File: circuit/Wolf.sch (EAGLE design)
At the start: 25 parts, among them IC1 74LS595N, IC2 24LC256P, K1 SNES, M1 ARDUINO-NANO-3.0

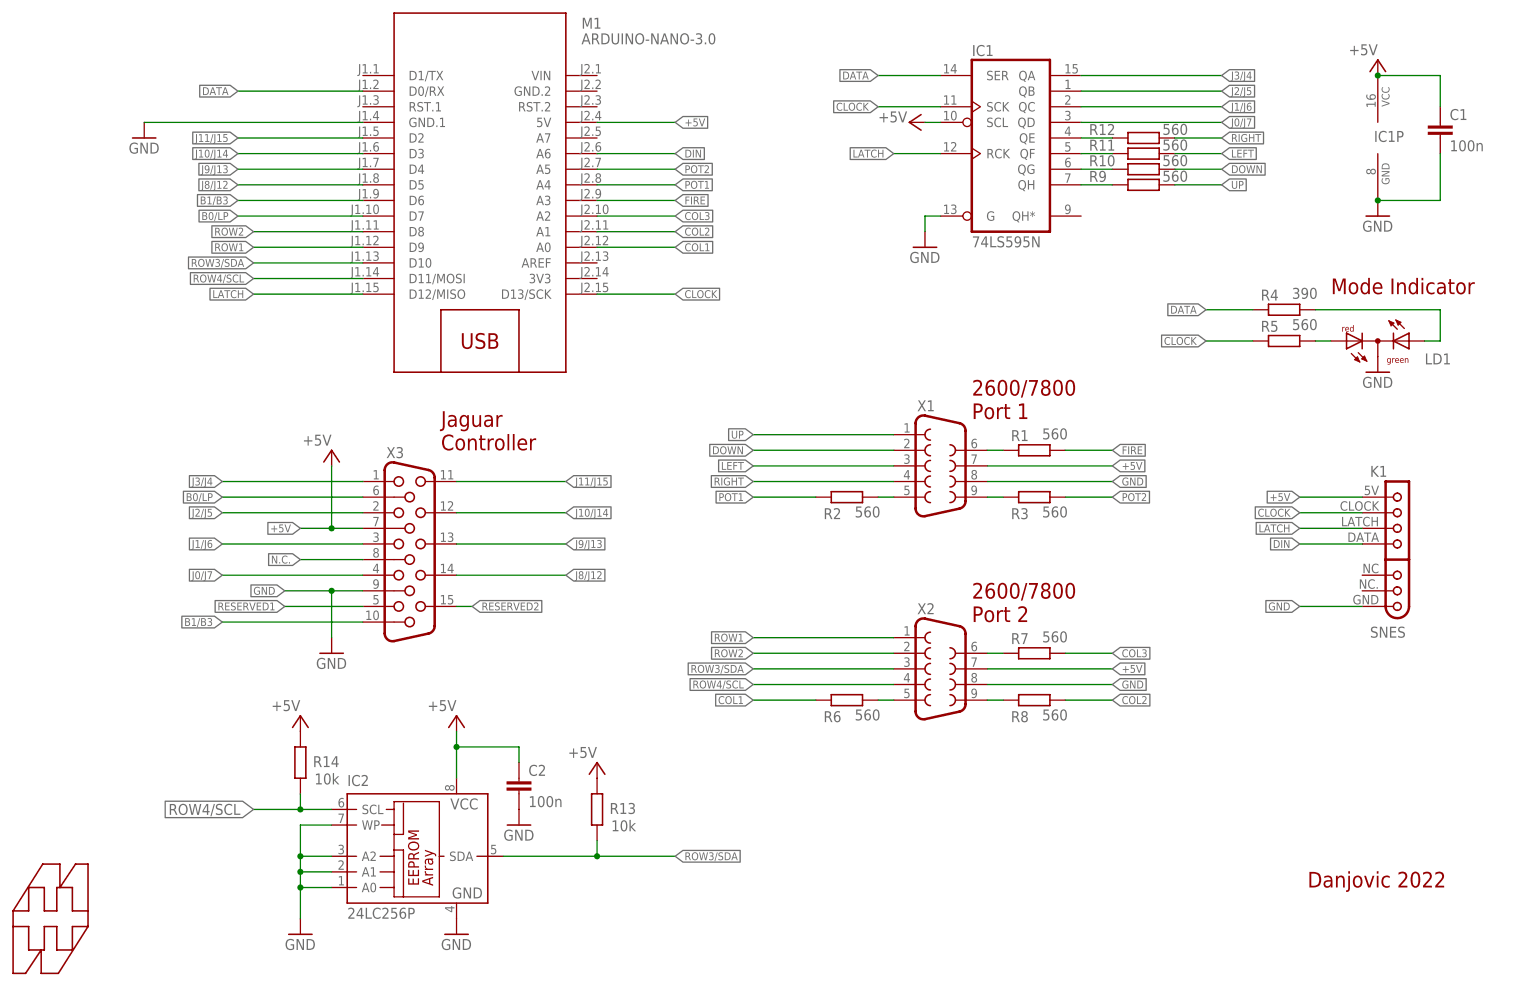
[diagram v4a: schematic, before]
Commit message: Added neopixel to indicate operating mode
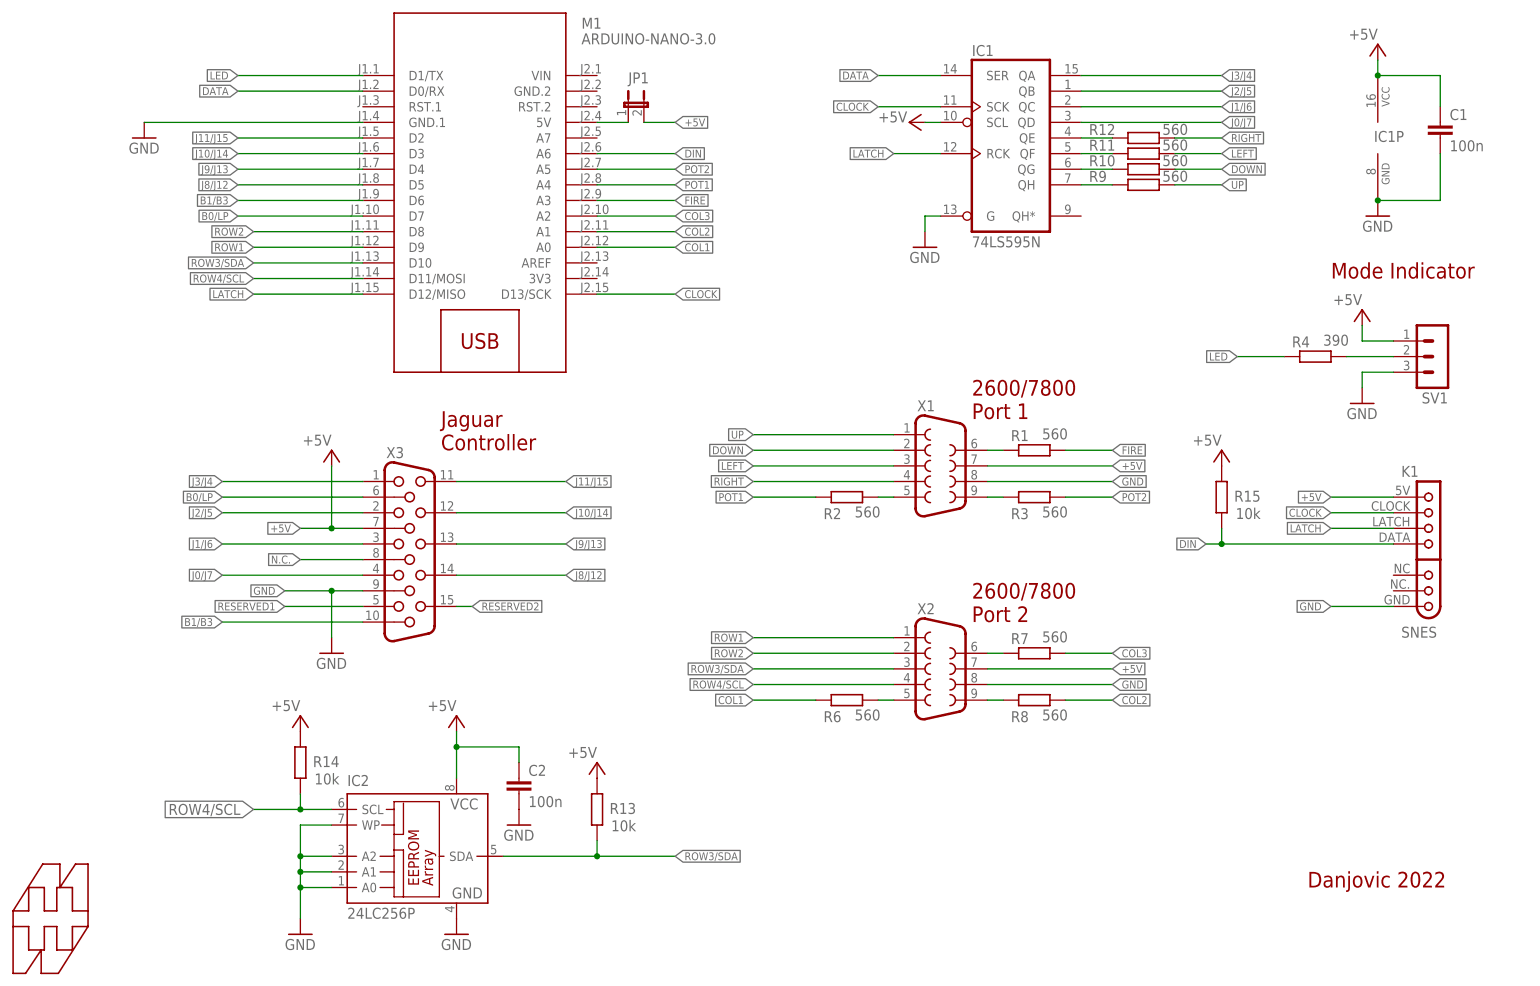
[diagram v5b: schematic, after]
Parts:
- removed LD1: (no value), led:DUOLED-RG-C
- removed R5: 560, rcl:R-EU_0204/7
- added JP1: (no value), jumper:JP1E
- added R15: 10k, rcl:R-EU_0204/7
- added SV1: (no value), con-lstb:MA03-1
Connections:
- removed net N$2: LD1.AR, R5.2
- new net LED: M1.D1/TX, R4.1
- new net VCC_ARD: JP1.1, M1.5V
- net +5V: now also JP1.2, R15.2, SV1.1; no longer M1.5V
- net CLOCK: no longer R5.1
- net DATA: no longer R4.1
- net DIN: now also R15.1
- net GND: now also SV1.3; no longer LD1.C
- net N$1: now also SV1.2; no longer LD1.AG
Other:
- moved on the sheet: K1, R4
